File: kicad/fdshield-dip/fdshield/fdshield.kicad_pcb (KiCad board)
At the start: 2 copper layers, 68.6 x 53.3 mm, 29 parts, among them J1 Conn_02x17_Odd_Even, P1 Power, P2 Analog, P3 Digital, P4 Digital, U1 74LS74, U3 74LS08, U4 74LS125, U5 23LCxxx, U6 74HCU04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

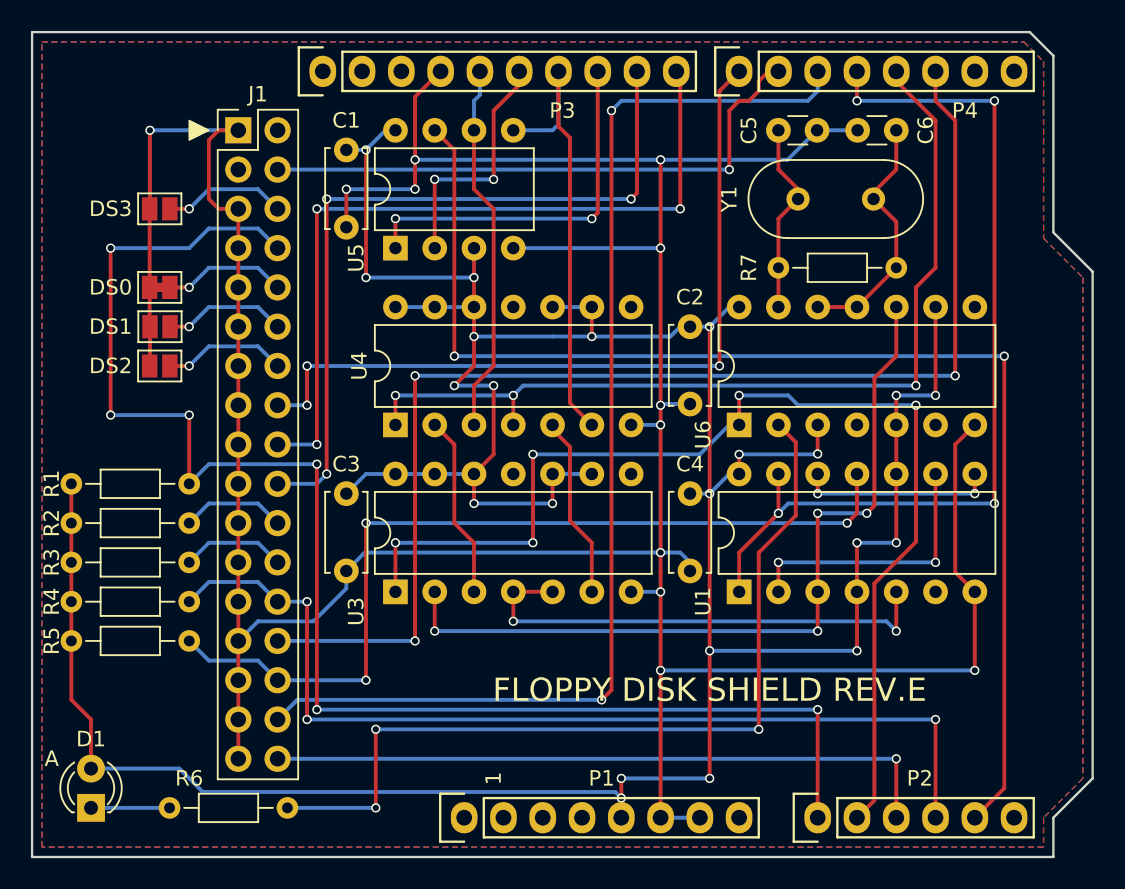
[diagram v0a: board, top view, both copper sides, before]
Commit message: PCB FAB-F. Add write back feature
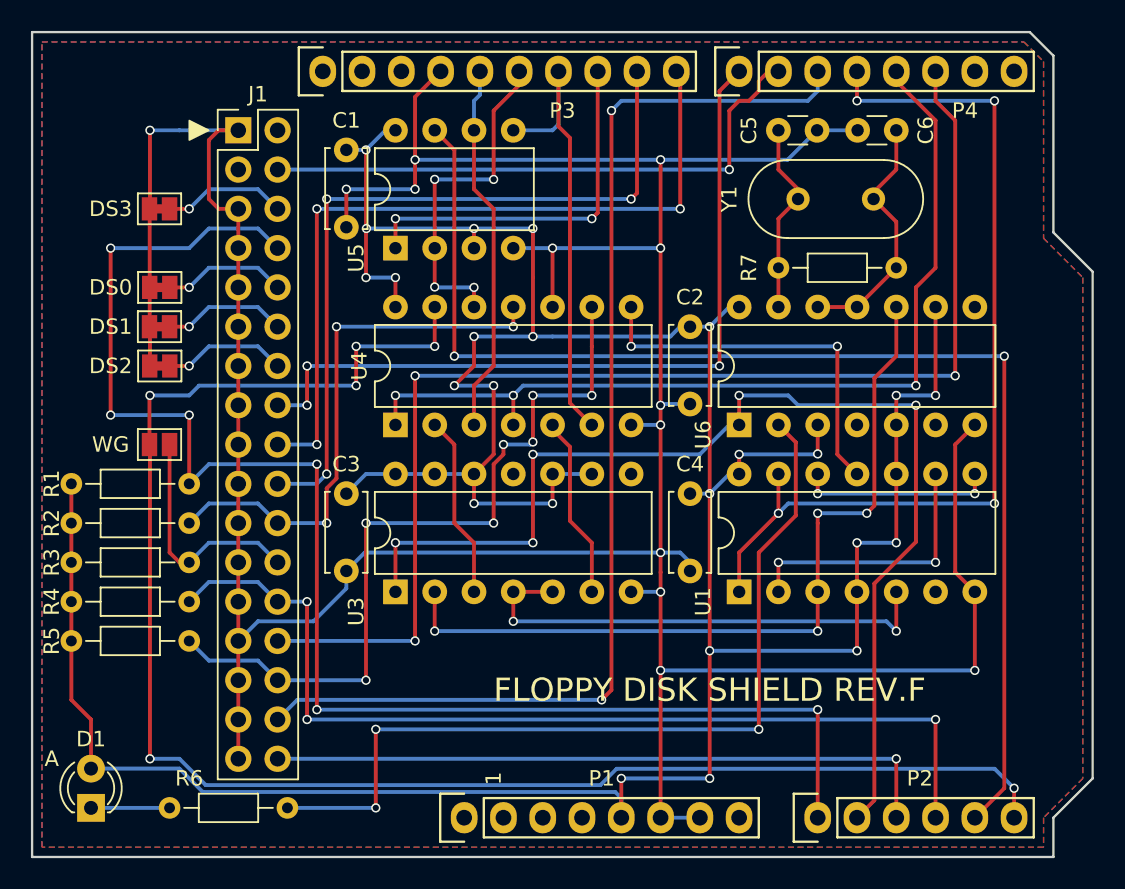
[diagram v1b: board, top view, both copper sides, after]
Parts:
- added WG: SolderJumper_2_Open, Jumper:SolderJumper-2_P1.3mm_Open_Pad1.0x1.5mm, F.Cu at (119.2, 99.7)
- DS1, DS2, DS3: value SolderJumper_2_Open -> SolderJumper_2_Bridged; footprint Jumper:SolderJumper-2_P1.3mm_Open_Pad1.0x1.5mm -> Jumper:SolderJumper-2_P1.3mm_Bridged_Pad1.0x1.5mm
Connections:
- P2 pad 6: (no net) -> /A5
- U1 pad 11: /RD -> Net-(U1-Pad11)
- U4 pad 10: +5V -> GND
- U4 pad 11: (no net) -> /WD
- U4 pad 12: +5V -> /12(MISO)
- U4 pad 13: +5V -> /A5
- U4 pad 8: (no net) -> Net-(U1-Pad11)
- U4 pad 9: +5V -> /RD
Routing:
- net /A5: track 0.00 -> 106.7 mm, vias 0 -> 6
- net /WD: track 6.77 -> 35.6 mm, vias 0 -> 3
- net Net-(U1-Pad11): track 0.00 -> 24.7 mm, vias 0 -> 2
- net /WG: track 6.77 -> 15.3 mm
- net /RD: track 57.2 -> 50.7 mm, vias 3 -> 7
- net /12(MISO): track 15.9 -> 22.3 mm, vias 2 -> 4
- net GND: track 240.0 -> 243.8 mm, vias 13 -> 14
- net +5V: track 226.3 -> 228.2 mm, vias 22 -> 24
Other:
- board text added: "FLOPPY DISK SHIELD REV.F"
- board text removed: "FLOPPY DISK SHIELD REV.E"

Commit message: daily commit
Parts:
- renumbered DS3 to JP1, DS0 to JP2, DS1 to JP3, DS2 to JP4, WG to JP5
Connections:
- U4 pad 10: GND -> +5V
- U4 pad 8: Net-(U1-Pad11) -> (no net)
- U4 pad 9: /RD -> +5V
- U6 pad 1: /A1 -> /RD
- U6 pad 2: Net-(R6-Pad2) -> Net-(U6-Pad2)
- U6 pad 3: +5V -> Net-(U6-Pad2)
- U6 pad 4: (no net) -> Net-(U6-Pad4)
- U6 pad 5: +5V -> Net-(U6-Pad4)
- U6 pad 6: (no net) -> Net-(U1-Pad11)
- U6 pad 8: (no net) -> Net-(R6-Pad2)
- U6 pad 9: +5V -> /A1
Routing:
- net Net-(R6-Pad2): track 56.7 -> 75.3 mm, vias 3 -> 5
- net +5V: track 228.2 -> 209.8 mm, vias 24 -> 22
- net Net-(U1-Pad11): track 24.7 -> 8.24 mm
- net GND: track 243.8 -> 240.0 mm, vias 14 -> 13
- net Net-(U6-Pad2): track 0.00 -> 3.17 mm
- net /RD: track 50.7 -> 53.4 mm, vias 7 -> 5
- net Net-(U6-Pad4): track 0.00 -> 2.54 mm
- net Net-(U1-Pad5): track 32.0 -> 31.1 mm
- net /A1: track 73.8 -> 73.2 mm, vias 5 -> 4
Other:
- board text added: "FLOPPY DISK SHIELD REV.G"
- board text removed: "FLOPPY DISK SHIELD REV.F"

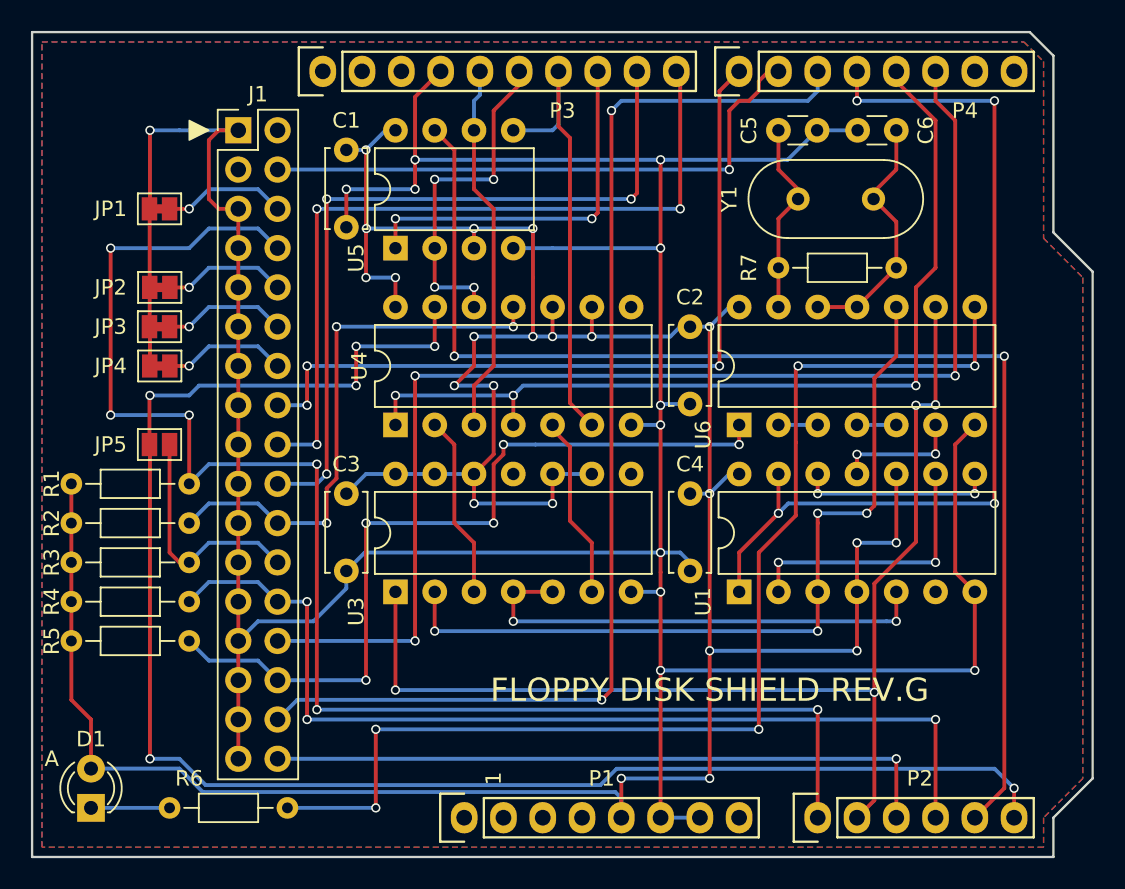
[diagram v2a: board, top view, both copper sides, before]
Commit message: JP5(WG) changed from solder jumper to pin header
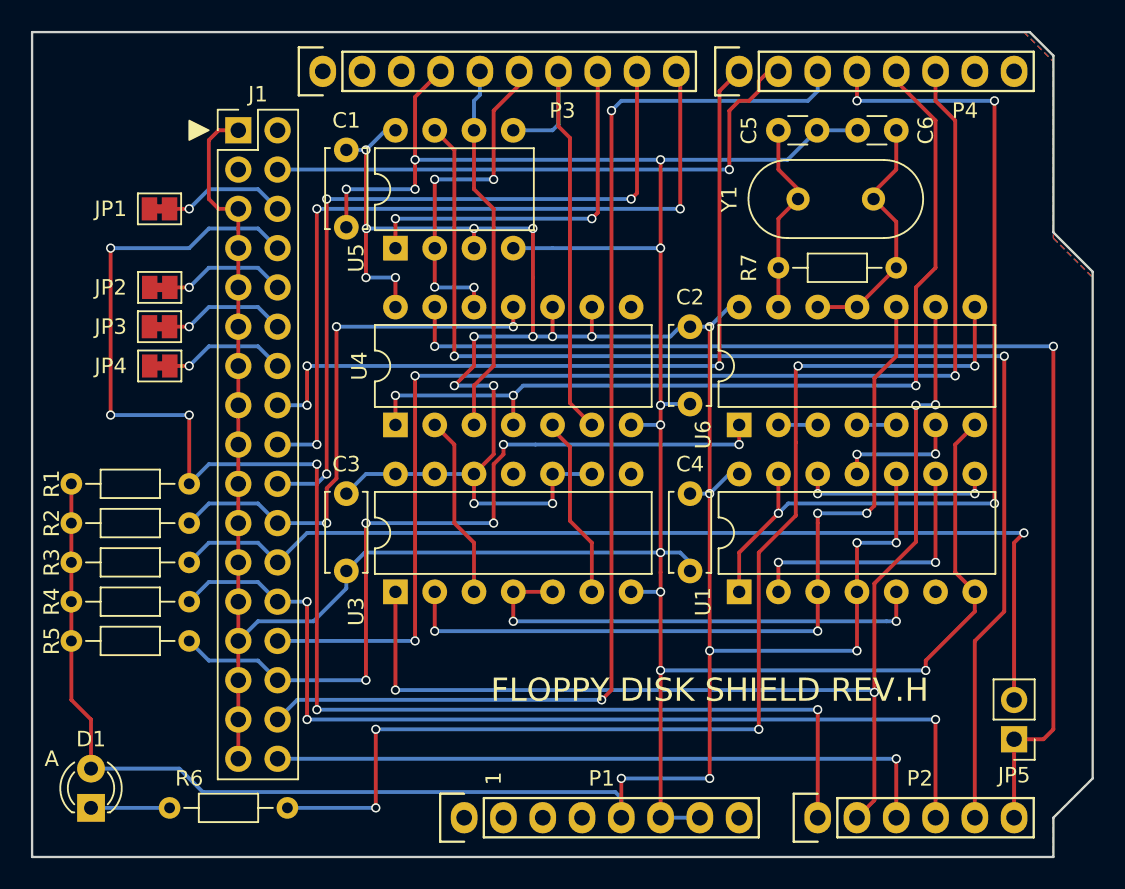
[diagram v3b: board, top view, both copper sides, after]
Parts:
- JP5: value SolderJumper_2_Open -> WRITE GATE; footprint Jumper:SolderJumper-2_P1.3mm_Open_Pad1.0x1.5mm -> Connector_PinHeader_2.54mm:PinHeader_1x02_P2.54mm_Vertical
- moved JP5 58.5 mm to (174.5, 118.8), turned to 180 degrees
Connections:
- net /10(**/SS) renamed /10(**/SS)
- net /11(**/MOSI) renamed /11(**/MOSI)
- J1 pad 2: (no net) -> unconnected-(J1-Pad2)
- J1 pad 3: (no net) -> unconnected-(J1-Pad3)
- P1 pad 1: (no net) -> unconnected-(P1-Pad1)
- P1 pad 2: (no net) -> /IOREF
- P1 pad 3: (no net) -> /Reset
- P1 pad 4: (no net) -> +3.3V
- P1 pad 8: (no net) -> /Vin
- P3 pad 1: (no net) -> unconnected-(P3-Pad1)
- P3 pad 2: (no net) -> unconnected-(P3-Pad2)
- P3 pad 3: (no net) -> /AREF
- P4 pad 7: (no net) -> /1(Tx)
- P4 pad 8: (no net) -> /0(Rx)
- U1 pad 6: (no net) -> unconnected-(U1-Pad6)
- U3 pad 11: (no net) -> unconnected-(U3-Pad11)
- U3 pad 8: (no net) -> unconnected-(U3-Pad8)
- U4 pad 8: (no net) -> unconnected-(U4-Pad8)
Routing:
- net /WG: track 15.3 -> 66.9 mm, vias 0 -> 1
- net /A5: track 106.7 -> 75.2 mm, vias 6 -> 2
- net GND: track 240.0 -> 217.1 mm, vias 13 -> 11
- net +5V: track 209.8 -> 209.2 mm
- net Net-(U6-Pad2): track 3.17 -> 2.54 mm
- net /RD: track 53.4 -> 52.8 mm
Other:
- net class Default removed
- board text added: "FLOPPY DISK SHIELD REV.H"
- board text removed: "FLOPPY DISK SHIELD REV.G"

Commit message: PCB data update (WG) (rev_h)
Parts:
- renumbered JP2 to DS0, JP3 to DS1, JP4 to DS2, JP1 to DS3
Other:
- board text added: "DRIVE SELECT"
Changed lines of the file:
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@@
     (property "Sheetname" "")
     (attr exclude_from_pos_files)
-    (fp_text reference "JP2" (at 3.175 0) (layer "F.SilkS")
+    (fp_text reference "DS0" (at 3.175 0) (layer "F.SilkS")
       (effects (font (size 1 1) (thickness 0.15)))
     )
@@
     (property "Sheetname" "")
     (attr exclude_from_pos_files)
-    (fp_text reference "JP4" (at 3.175 0) (layer "F.SilkS")
+    (fp_text reference "DS2" (at 3.175 0) (layer "F.SilkS")
       (effects (font (size 1 1) (thickness 0.15)))
     )
@@
     (property "Sheetname" "")
     (attr exclude_from_pos_files)
-    (fp_text reference "JP1" (at 3.16 0) (layer "F.SilkS")
+    (fp_text reference "DS3" (at 3.16 0) (layer "F.SilkS")
       (effects (font (size 1 1) (thickness 0.15)))
     )
@@
     (property "Sheetname" "")
     (attr exclude_from_pos_files)
-    (fp_text reference "JP3" (at 3.16 0) (layer "F.SilkS")
+    (fp_text reference "DS1" (at 3.16 0) (layer "F.SilkS")
       (effects (font (size 1 1) (thickness 0.15)))
     )
@@
       (effects (font (size 1 1) (thickness 0.15)))
     )
-    (fp_text value "WRITE GATE" (at -3.175 1.91 90) (layer "F.Fab")
+    (fp_text value "WRITE GATE" (at -3.175 1.91 90) (layer "F.SilkS")
       (effects (font (size 1 1) (thickness 0.15)))
     )
@@
     (effects (font (size 1 1) (thickness 0.15)))
   )
-  (gr_text "FLOPPY DISK SHIELD REV.H" (at 154.813 115.57) (layer "F.SilkS")
+  (gr_text "FLOPPY DISK SHIELD REV.H" (at 151.638 114.935) (layer "F.SilkS")
     (effects (font (size 1.5 1.5) (thickness 0.25)))
   )
+  (gr_text "DRIVE SELECT" (at 113.538 89.535 90) (layer "F.SilkS")
+    (effects (font (size 1 1) (thickness 0.15)))
+  )
   (gr_text "A" (at 112.268 120.015) (layer "F.SilkS")
